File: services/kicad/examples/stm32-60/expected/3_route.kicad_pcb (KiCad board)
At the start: 2 copper layers, 132 x 99 mm, 60 parts, among them J1 5V, U1 STM32F103C8T6, U2 AMS1117-3.3

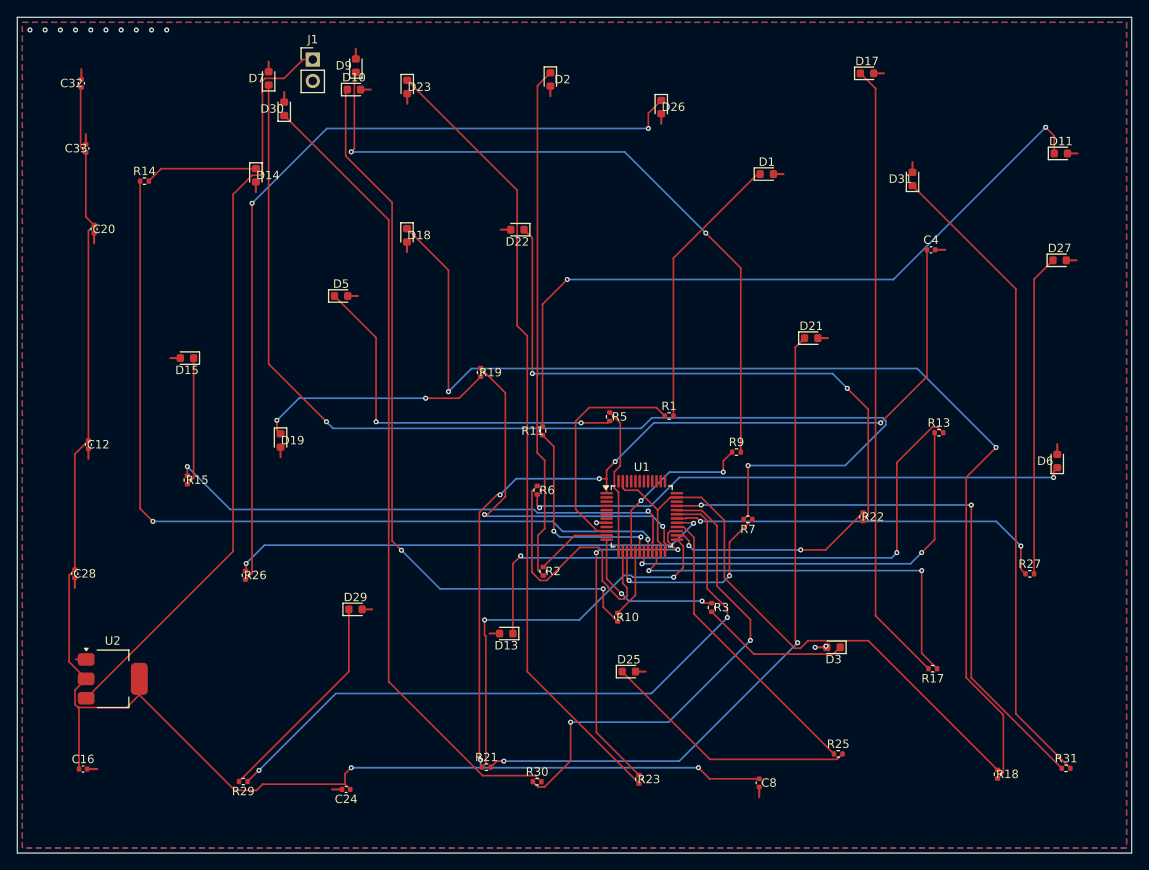
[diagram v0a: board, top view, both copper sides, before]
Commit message: feat(kicad): placement pro et routage 100 % fabricable sur les 16 cartes -- integration sur main (#164)
Branche d'integration coupee depuis origin/main (fab2a82, PR #162) : les
fichiers cles de main etaient des instantanes de feat/placement-seed-snap-
bypass (routing.py = 7981019, placement.py = 437a8b4...). On reprend donc
l'arbre entier de cette branche (345 commits, dernier 9f48667) et on y
conserve ce que main seul apportait :
- tools/verrou_routage.py + son test : « 6,2 Go par routage » rectifie
  (0,2 Go mesure ; c'est la concurrence qui emballe la memoire) ;
- tests/test_driver_llm_resync.py ;
- CLAUDE.md, PLAN.md, DECISIONS.md : fusion a trois voies, les sections
  des deux lignes conservees (2026-09-05 conteneur/verrou, 2026-09-07
  parcours asynchrone et chaine du driver, 2026-09-09/10 lecons).
Les skills *-delegate restent supprimes (remplaces le 2026-08-30).

Contenu : banc en deux phases (placement valide puis routage gele), snap
sur les regles natives, repli GND cible, journal Freerouting incremental,
horloge sans progres, via d'echappement vers le plan principal,
serigraphie degagee ; 16 cartes livrees a 100 %, 0 erreur DRC.

Verification : pytest services/kicad 1805 passed, 16 skipped ;
pnpm type-check 8/8.


Claude-Session: https://claude.ai/code/session_01TnMqm4La2CxQHHB5K8aSSV

Co-authored-by: Claude Fable 5.1 <noreply@anthropic.com>
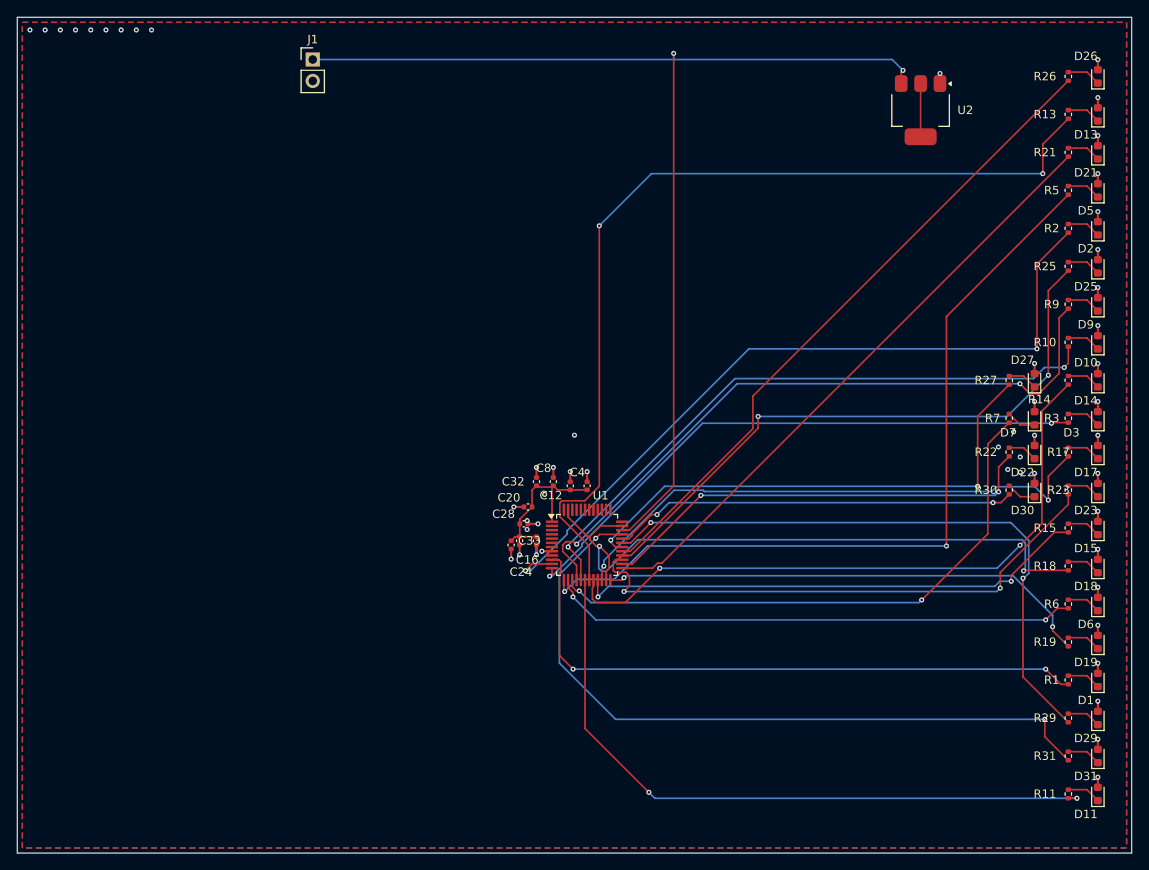
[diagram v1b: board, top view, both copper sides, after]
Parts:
- moved U2 117.0 mm to (189.5, 66.5), turned to -90 degrees
- moved R26 114.0 mm to (207.0, 62.5), turned to 90 degrees
- moved R14 112.0 mm to (207.0, 98.5), turned to 90 degrees
- moved D15 109.8 mm to (210.5, 116.0), turned to 90 degrees
- moved R15 104.5 mm to (207.0, 116.0), turned to 90 degrees
- moved D14 102.7 mm to (210.5, 98.5), turned to 90 degrees
- moved R21 100.3 mm to (207.0, 71.5), turned to 90 degrees
- moved D19 99.7 mm to (210.5, 129.5), turned to 90 degrees
- moved D30 99.7 mm to (203.0, 111.5)
- moved D7 99.3 mm to (203.0, 103.0)
- moved R29 98.0 mm to (207.0, 138.5), turned to 90 degrees
- moved D23 94.7 mm to (210.5, 111.5), turned to 90 degrees
- moved D13 93.2 mm to (210.5, 67.0), turned to 90 degrees
- moved D10 93.1 mm to (210.5, 94.0), turned to 90 degrees
- moved D9 92.3 mm to (210.5, 89.5)
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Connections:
- C12 pad 1: +3.3V -> +3V3
- C16 pad 1: +3.3V -> +3V3
- C20 pad 1: +3.3V -> +3V3
- C24 pad 1: +3.3V -> +3V3
- C28 pad 1: +3.3V -> +3V3
- C32 pad 1: +3.3V -> +3V3
- C33 pad 1: +3.3V -> +3V3
- C4 pad 1: +3.3V -> +3V3
- C8 pad 1: +3.3V -> +3V3
- U1 pad 1: +3.3V -> +3V3
- U1 pad 34: Net-(U1-34) -> VIN
- U2 pad 2: +3.3V -> Net-(U2-2)
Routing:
- net +3.3V: track 282.6 -> 0.00 mm, vias 7 -> 0
- net LED7: track 135.4 -> 3.54 mm, vias 2 -> 0
- net LED18: track 134.0 -> 4.04 mm, vias 2 -> 0
- net LED26: track 99.5 -> 4.04 mm, vias 2 -> 0
- net LED30: track 95.2 -> 3.54 mm
- net LED23: track 94.7 -> 4.04 mm
- net LED10: track 87.8 -> 4.04 mm, vias 2 -> 0
- net LED11: track 86.3 -> 4.04 mm, vias 2 -> 0
- net GPIO2: track 9.06 -> 90.5 mm, vias 0 -> 2
- net LED9: track 83.3 -> 4.04 mm, vias 2 -> 0
- net GPIO5: track 17.5 -> 96.5 mm, vias 0 -> 2
- net LED21: track 79.1 -> 4.04 mm, vias 2 -> 0
- net LED31: track 76.8 -> 4.04 mm
- net LED17: track 73.9 -> 4.04 mm
- net LED22: track 72.5 -> 3.54 mm, vias 2 -> 0
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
